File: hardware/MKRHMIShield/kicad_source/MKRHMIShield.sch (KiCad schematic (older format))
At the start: 29 parts, among them CN1 ARDUINO_MKR, Q1 2N7002, SW1 TAST_VER, SW2 TAST_VER, SW3 TAST_VER, SW4 TAST_VER, SW5 TAST_VER, SW6 TAST_VER

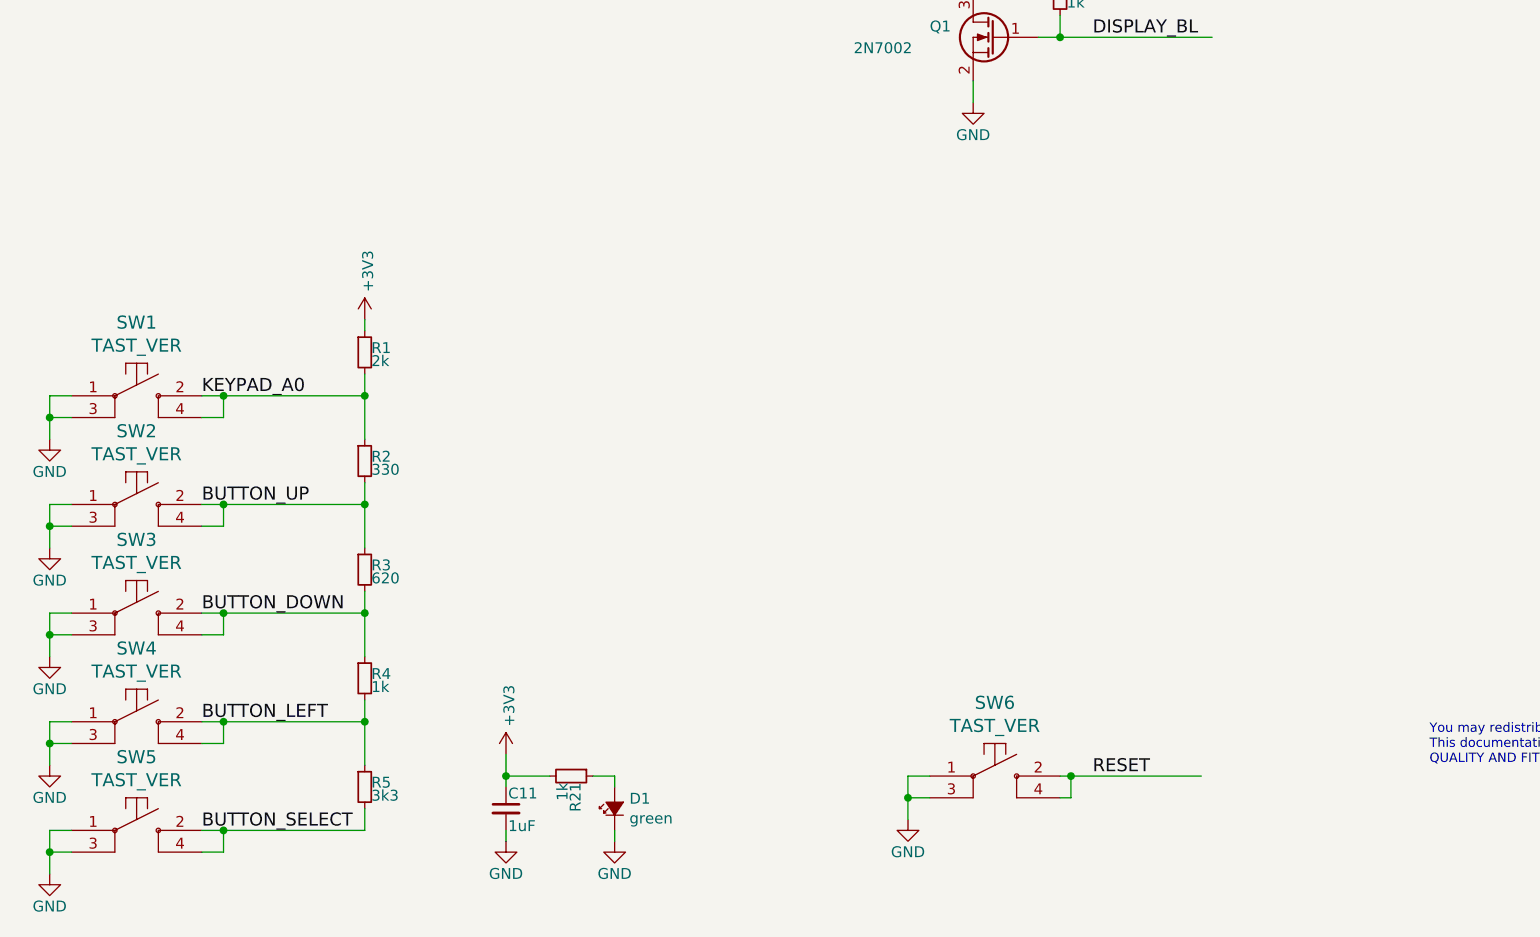
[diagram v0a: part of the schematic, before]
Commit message: exchanged switches with a joystick
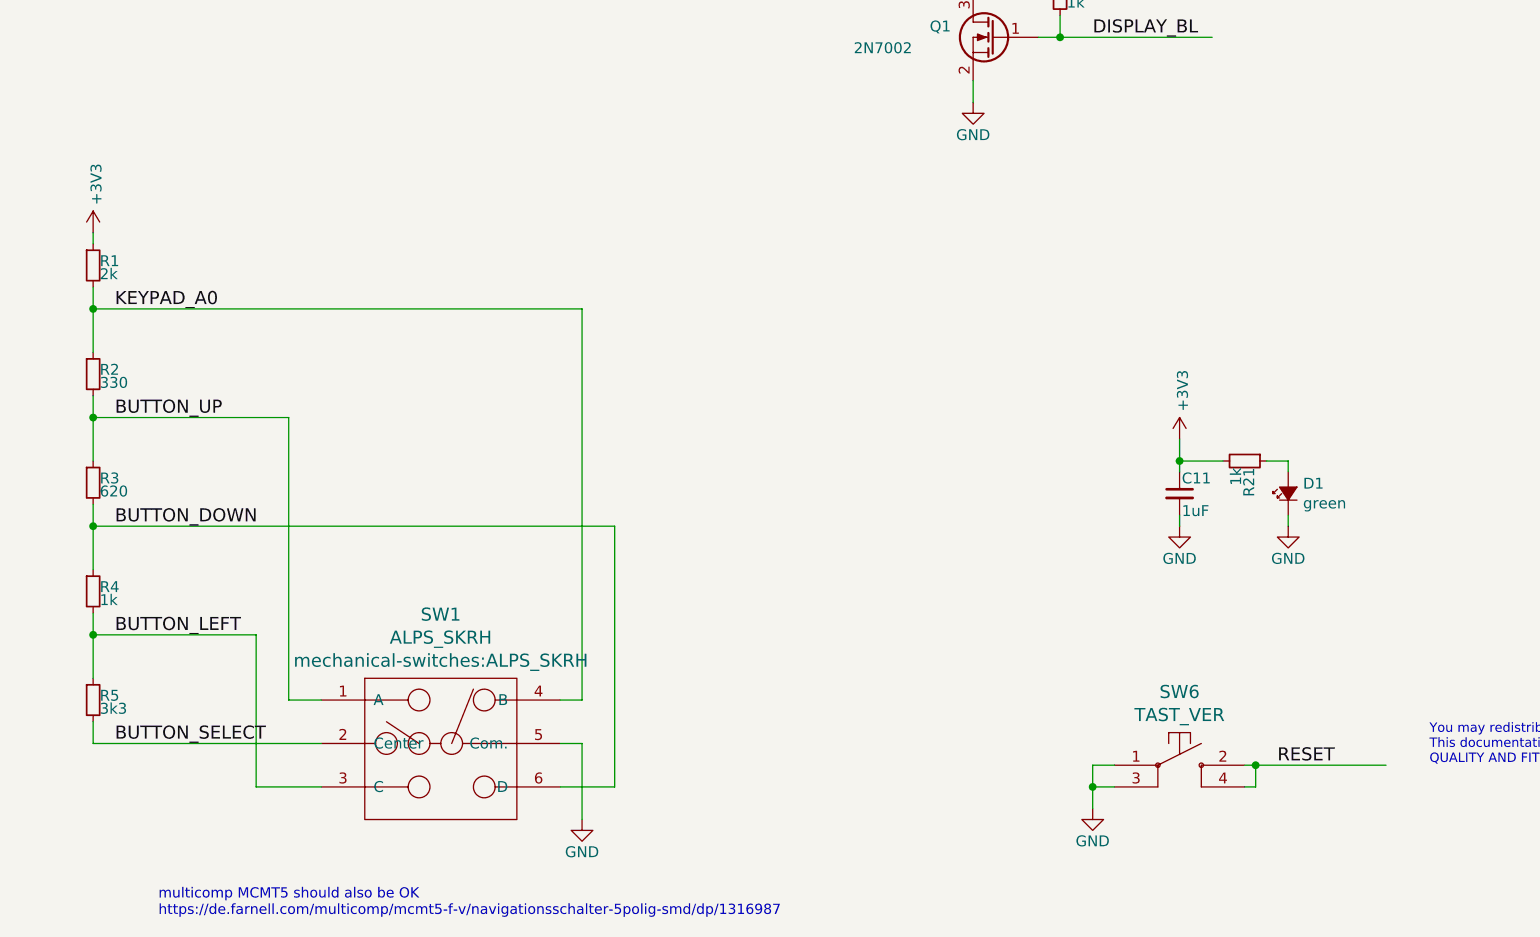
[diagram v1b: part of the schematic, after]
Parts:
- removed SW1, SW2, SW3, SW4, SW5: TAST_VER, mechanical-switches:WE_430182080816, symbol MKRHMIShield-rescue:TAST_VER-mechanical-switches-MKRHMIShield-rescue
- added SW1: ALPS_SKRH, mechanical-switches:ALPS_SKRH, symbol mechanical-switches:ALPS_SKRH
- CN1: footprint MODULE_compute:ARDUINO_MKR -> MODULE_compute:ARDUINO_MKR_HOLES
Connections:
- wire segments 139 -> 114
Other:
- note added: "multicomp MCMT5 should also be OK\nhttps://de.farnell.com/multicomp/mcmt5-f-v/navigationsschalter-5polig-smd/dp/1316987"
- moved on the sheet: C11, D1, R1, R2, R21, R3, R4, R5, SW6
